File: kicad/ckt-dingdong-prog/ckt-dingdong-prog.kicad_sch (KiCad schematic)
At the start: 5 parts, among them J1 Conn_02x05_Counter_Clockwise, J2 Conn_AVR_TagConnect_TC2030, J3 Conn_01x11, J4 Conn_01x11, SW1 JS202011SCQN

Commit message: Programming board PCB complete
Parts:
- J3, J4: footprint (none) -> Connector_PinHeader_2.54mm:PinHeader_1x11_P2.54mm_Vertical
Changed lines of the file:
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@@
   (symbol (lib_id "power:GND") (at 63.5 96.52 0) (unit 1)
     (in_bom yes) (on_board yes)
-    (property "Reference" "#PWR?" (id 0) (at 63.5 102.87 0)
+    (property "Reference" "#PWR0104" (id 0) (at 63.5 102.87 0)
       (effects (font (size 1.27 1.27)) hide)
     )
@@
     (property "Reference" "J4" (id 0) (at 196.215 74.295 0))
     (property "Value" "Conn_01x11" (id 1) (at 196.215 76.835 0))
-    (property "Footprint" "" (id 2) (at 196.215 92.71 0)
+    (property "Footprint" "Connector_PinHeader_2.54mm:PinHeader_1x11_P2.54mm_Vertical" (id 2) (at 196.215 92.71 0)
       (effects (font (size 1.27 1.27)) hide)
     )
@@
   (symbol (lib_id "power:+3.3V") (at 169.545 78.74 0) (unit 1)
     (in_bom yes) (on_board yes)
-    (property "Reference" "#PWR?" (id 0) (at 169.545 82.55 0)
+    (property "Reference" "#PWR0106" (id 0) (at 169.545 82.55 0)
       (effects (font (size 1.27 1.27)) hide)
     )
@@
   (symbol (lib_id "power:GND") (at 109.855 95.25 0) (unit 1)
     (in_bom yes) (on_board yes)
-    (property "Reference" "#PWR?" (id 0) (at 109.855 101.6 0)
+    (property "Reference" "#PWR0102" (id 0) (at 109.855 101.6 0)
       (effects (font (size 1.27 1.27)) hide)
     )
@@
       (effects (font (size 1.27 1.27)) (justify left))
     )
-    (property "Footprint" "" (id 2) (at 179.07 92.71 0)
+    (property "Footprint" "Connector_PinHeader_2.54mm:PinHeader_1x11_P2.54mm_Vertical" (id 2) (at 179.07 92.71 0)
       (effects (font (size 1.27 1.27)) hide)
     )
@@
   (symbol (lib_id "power:GND") (at 78.105 120.015 0) (mirror y) (unit 1)
     (in_bom yes) (on_board yes)
-    (property "Reference" "#PWR?" (id 0) (at 78.105 126.365 0)
+    (property "Reference" "#PWR0101" (id 0) (at 78.105 126.365 0)
       (effects (font (size 1.27 1.27)) hide)
     )
@@
   (symbol (lib_id "power:+3.3V") (at 63.5 76.2 0) (unit 1)
     (in_bom yes) (on_board yes)
-    (property "Reference" "#PWR?" (id 0) (at 63.5 80.01 0)
+    (property "Reference" "#PWR0105" (id 0) (at 63.5 80.01 0)
       (effects (font (size 1.27 1.27)) hide)
     )
@@
   (symbol (lib_id "power:GND") (at 170.815 85.09 270) (unit 1)
     (in_bom yes) (on_board yes)
-    (property "Reference" "#PWR?" (id 0) (at 164.465 85.09 0)
+    (property "Reference" "#PWR0107" (id 0) (at 164.465 85.09 0)
       (effects (font (size 1.27 1.27)) hide)
     )
@@
   (symbol (lib_id "power:+3.3V") (at 109.855 82.55 0) (unit 1)
     (in_bom yes) (on_board yes)
-    (property "Reference" "#PWR?" (id 0) (at 109.855 86.36 0)
+    (property "Reference" "#PWR0103" (id 0) (at 109.855 86.36 0)
       (effects (font (size 1.27 1.27)) hide)
     )
@@
   (symbol (lib_id "power:GND") (at 204.47 80.01 90) (mirror x) (unit 1)
     (in_bom yes) (on_board yes)
-    (property "Reference" "#PWR?" (id 0) (at 210.82 80.01 0)
+    (property "Reference" "#PWR0108" (id 0) (at 210.82 80.01 0)
       (effects (font (size 1.27 1.27)) hide)
     )
@@
   )
   (symbol_instances
+    (path "/ac5e832f-5605-4361-b104-da0c11386df5"
+      (reference "#PWR0101") (unit 1) (value "GND") (footprint "")
+    )
+    (path "/89dfde83-0d62-45cd-b799-a7d2e3d1022f"
+      (reference "#PWR0102") (unit 1) (value "GND") (footprint "")
+    )
+    (path "/d3241dde-1c6a-4b3c-95fc-28b0e3d1ac80"
+      (reference "#PWR0103") (unit 1) (value "+3.3V") (footprint "")
+    )
     (path "/0b9acb28-32d4-442e-9524-2d3eb05627b8"
-      (reference "#PWR?") (unit 1) (value "GND") (footprint "")
+      (reference "#PWR0104") (unit 1) (value "GND") (footprint "")
+    )
+    (path "/c6647ba0-c558-4447-9e8b-33e9e0feb743"
+      (reference "#PWR0105") (unit 1) (value "+3.3V") (footprint "")
     )
     (path "/758fb082-f9c9-402b-b437-3ba76bb58b5f"
-      (reference "#PWR?") (unit 1) (value "+3.3V") (footprint "")
-    )
-    (path "/89dfde83-0d62-45cd-b799-a7d2e3d1022f"
-      (reference "#PWR?") (unit 1) (value "GND") (footprint "")
-    )
-    (path "/ac5e832f-5605-4361-b104-da0c11386df5"
-      (reference "#PWR?") (unit 1) (value "GND") (footprint "")
-    )
-    (path "/c6647ba0-c558-4447-9e8b-33e9e0feb743"
-      (reference "#PWR?") (unit 1) (value "+3.3V") (footprint "")
+      (reference "#PWR0106") (unit 1) (value "+3.3V") (footprint "")
     )
     (path "/c715221c-9e91-48a6-9aea-e37fd69b179b"
-      (reference "#PWR?") (unit 1) (value "GND") (footprint "")
-    )
-    (path "/d3241dde-1c6a-4b3c-95fc-28b0e3d1ac80"
-      (reference "#PWR?") (unit 1) (value "+3.3V") (footprint "")
+      (reference "#PWR0107") (unit 1) (value "GND") (footprint "")
     )
     (path "/e29628f6-5145-4926-87fe-69f2c0894165"
-      (reference "#PWR?") (unit 1) (value "GND") (footprint "")
+      (reference "#PWR0108") (unit 1) (value "GND") (footprint "")
     )
     (path "/5f39442f-fdeb-4900-b9f4-b34ab407a918"
@@
     )
     (path "/a30fa920-d39f-4c3f-8180-704f1a85a554"
-      (reference "J3") (unit 1) (value "Conn_01x11") (footprint "")
+      (reference "J3") (unit 1) (value "Conn_01x11") (footprint "Connector_PinHeader_2.54mm:PinHeader_1x11_P2.54mm_Vertical")
     )
     (path "/1cfdb6c4-1482-404e-900f-738ccb5046ef"
-      (reference "J4") (unit 1) (value "Conn_01x11") (footprint "")
+      (reference "J4") (unit 1) (value "Conn_01x11") (footprint "Connector_PinHeader_2.54mm:PinHeader_1x11_P2.54mm_Vertical")
     )
     (path "/4bc4b1ea-398b-4e60-a693-362841a5cba9"

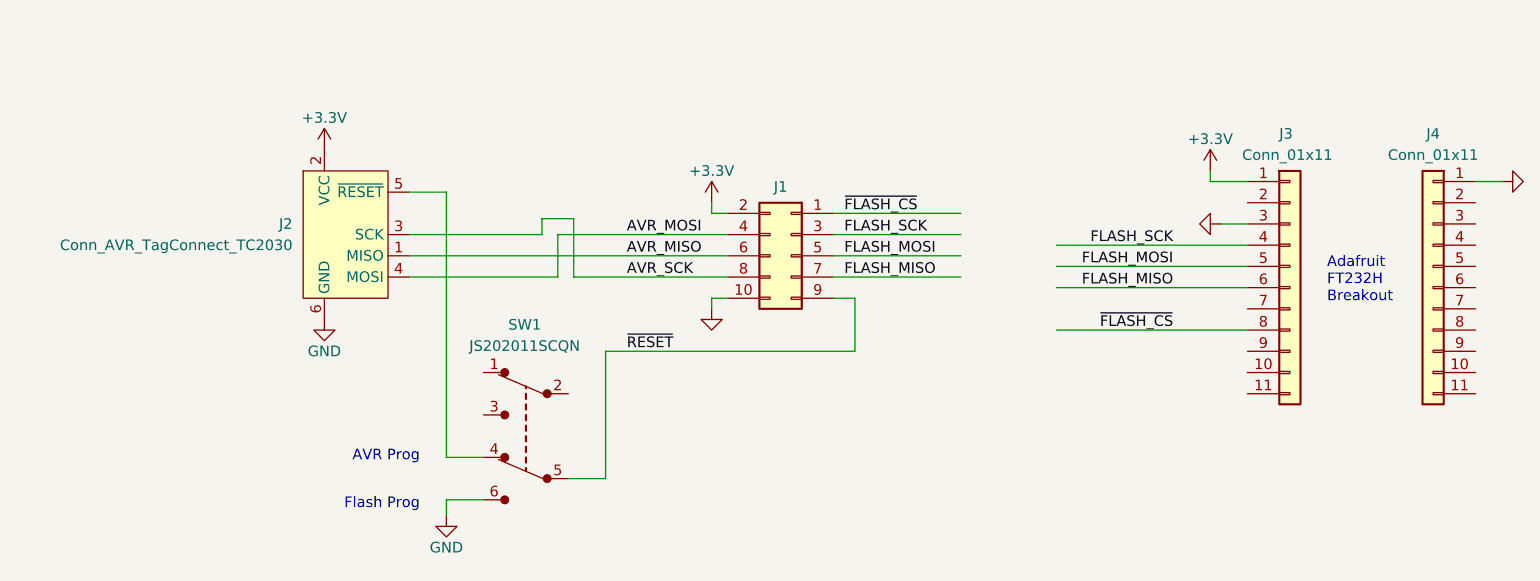
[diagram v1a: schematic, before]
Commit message: Fixed programming header
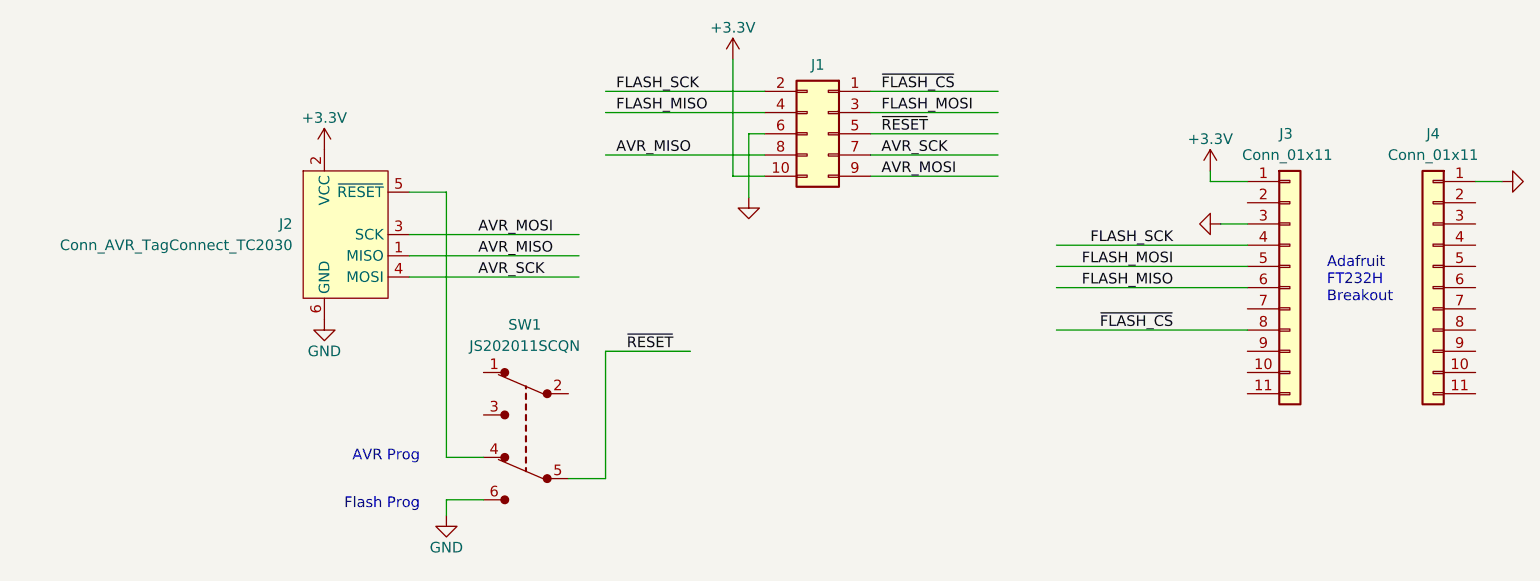
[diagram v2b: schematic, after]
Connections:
- net +3.3V: now also J1.10 (Pin_10); no longer J1.2 (Pin_2)
- net AVR_MISO: now also J1.8 (Pin_8); no longer J1.6 (Pin_6)
- net AVR_MOSI: now also J1.9 (Pin_9), J2.3 (SCK); no longer J1.4 (Pin_4), J2.4 (MOSI)
- net AVR_SCK: now also J1.7 (Pin_7), J2.4 (MOSI); no longer J1.8 (Pin_8), J2.3 (SCK)
- net FLASH_MISO: now also J1.4 (Pin_4); no longer J1.7 (Pin_7)
- net FLASH_MOSI: now also J1.3 (Pin_3); no longer J1.5 (Pin_5)
- net FLASH_SCK: now also J1.2 (Pin_2); no longer J1.3 (Pin_3)
- net GND: now also J1.6 (Pin_6); no longer J1.10 (Pin_10)
- net ~{RESET}: now also J1.5 (Pin_5); no longer J1.9 (Pin_9)

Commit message: Update programmer to fix SCK / MISO reversal, now v1.2
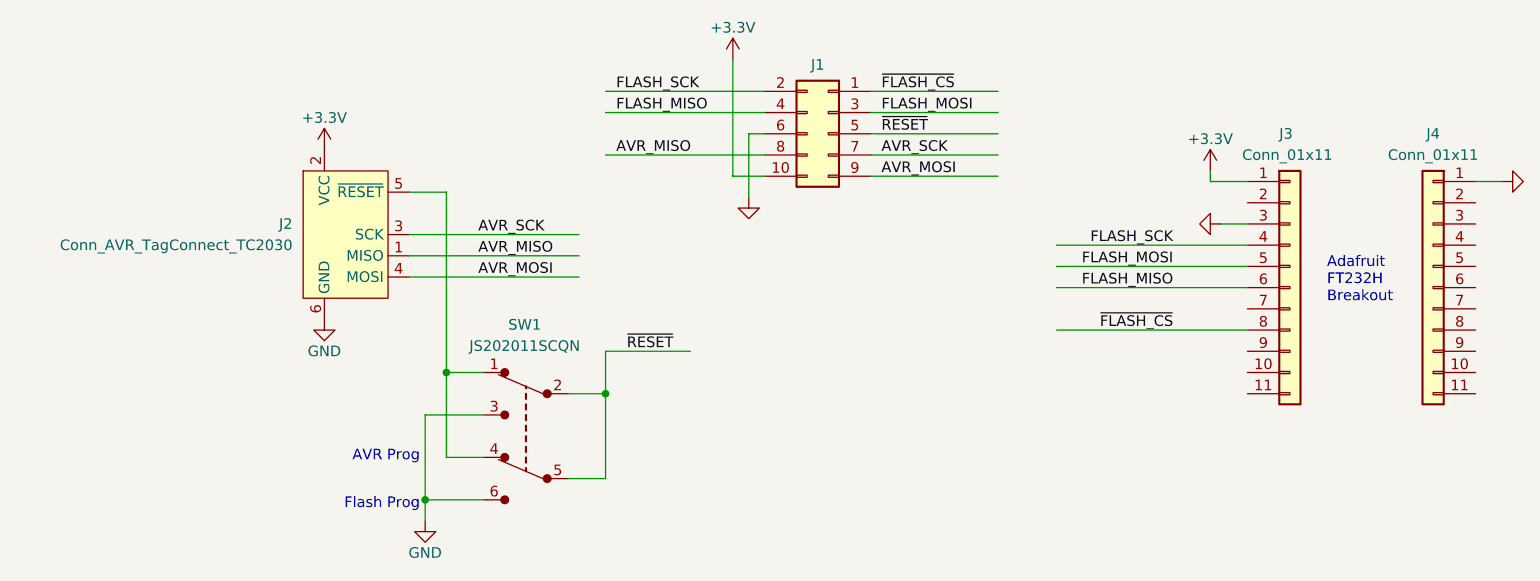
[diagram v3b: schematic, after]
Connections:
- net AVR_MOSI: now also J2.4 (MOSI); no longer J2.3 (SCK)
- net AVR_SCK: now also J2.3 (SCK); no longer J2.4 (MOSI)
- net GND: now also SW1.3
- net ~{RESET}: now also SW1.2
- net at SW1.1: now also J2.5 (~{RESET}), SW1.4
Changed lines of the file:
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@@
 (kicad_sch (version 20211123) (generator eeschema)
   (paper "A4")
+  (junction (at 75.565 118.11) (diameter 0) (color 0 0 0 0)
+  )
+  (junction (at 78.105 102.87) (diameter 0) (color 0 0 0 0)
+  )
+  (junction (at 97.155 105.41) (diameter 0) (color 0 0 0 0)
+  )
   (wire (pts (xy 112.395 65.405) (xy 112.395 79.375))
     (stroke (width 0) (type default) (color 0 0 0 0))
@@
     (stroke (width 0) (type default) (color 0 0 0 0))
   )
+  (wire (pts (xy 97.155 105.41) (xy 97.155 115.57))
+    (stroke (width 0) (type default) (color 0 0 0 0))
+  )
   (wire (pts (xy 169.545 78.74) (xy 169.545 80.01))
     (stroke (width 0) (type default) (color 0 0 0 0))
   )
+  (wire (pts (xy 78.105 102.87) (xy 78.105 113.03))
+    (stroke (width 0) (type default) (color 0 0 0 0))
+  )
+  (wire (pts (xy 78.105 102.87) (xy 82.55 102.87))
+    (stroke (width 0) (type default) (color 0 0 0 0))
+  )
   (wire (pts (xy 114.3 74.295) (xy 116.205 74.295))
     (stroke (width 0) (type default) (color 0 0 0 0))
@@
     (stroke (width 0) (type default) (color 0 0 0 0))
   )
+  (wire (pts (xy 92.71 105.41) (xy 97.155 105.41))
+    (stroke (width 0) (type default) (color 0 0 0 0))
+  )
+  (wire (pts (xy 75.565 107.95) (xy 82.55 107.95))
+    (stroke (width 0) (type default) (color 0 0 0 0))
+  )
   (wire (pts (xy 112.395 79.375) (xy 116.205 79.375))
     (stroke (width 0) (type default) (color 0 0 0 0))
@@
     (stroke (width 0) (type default) (color 0 0 0 0))
   )
-  (wire (pts (xy 78.105 81.28) (xy 78.105 113.03))
+  (wire (pts (xy 75.565 118.11) (xy 75.565 107.95))
+    (stroke (width 0) (type default) (color 0 0 0 0))
+  )
+  (wire (pts (xy 78.105 81.28) (xy 78.105 102.87))
     (stroke (width 0) (type default) (color 0 0 0 0))
   )
@@
     (stroke (width 0) (type default) (color 0 0 0 0))
   )
-  (wire (pts (xy 78.105 118.11) (xy 78.105 120.015))
-    (stroke (width 0) (type default) (color 0 0 0 0))
-  )
   (wire (pts (xy 128.905 69.215) (xy 144.145 69.215))
     (stroke (width 0) (type default) (color 0 0 0 0))
   )
-  (wire (pts (xy 78.105 118.11) (xy 82.55 118.11))
+  (wire (pts (xy 75.565 120.65) (xy 75.565 118.11))
+    (stroke (width 0) (type default) (color 0 0 0 0))
+  )
+  (wire (pts (xy 75.565 118.11) (xy 82.55 118.11))
     (stroke (width 0) (type default) (color 0 0 0 0))
   )
@@
     (stroke (width 0) (type default) (color 0 0 0 0))
   )
-  (wire (pts (xy 97.155 100.33) (xy 97.155 115.57))
+  (wire (pts (xy 97.155 100.33) (xy 97.155 105.41))
     (stroke (width 0) (type default) (color 0 0 0 0))
   )
@@
     (effects (font (size 1.27 1.27)) (justify left bottom))
   )
-  (label "AVR_MOSI" (at 81.915 86.36 0)
+  (label "AVR_SCK" (at 81.915 86.36 0)
     (effects (font (size 1.27 1.27)) (justify left bottom))
   )
@@
     (effects (font (size 1.27 1.27)) (justify left bottom))
   )
-  (label "AVR_SCK" (at 81.915 91.44 0)
+  (label "AVR_MOSI" (at 81.915 91.44 0)
     (effects (font (size 1.27 1.27)) (justify left bottom))
   )
@@
     (pin "9")
   )
-  (symbol (lib_id "power:GND") (at 78.105 120.015 0) (mirror y) (unit 1)
-    (in_bom yes) (on_board yes)
-    (property "Reference" "#PWR0101" (id 0) (at 78.105 126.365 0)
-      (effects (font (size 1.27 1.27)) hide)
-    )
-    (property "Value" "GND" (id 1) (at 78.105 123.825 0))
-    (property "Footprint" "" (id 2) (at 78.105 120.015 0)
-      (effects (font (size 1.27 1.27)) hide)
-    )
-    (property "Datasheet" "" (id 3) (at 78.105 120.015 0)
+  (symbol (lib_id "power:GND") (at 75.565 120.65 0) (mirror y) (unit 1)
+    (in_bom yes) (on_board yes)
+    (property "Reference" "#PWR0101" (id 0) (at 75.565 127 0)
+      (effects (font (size 1.27 1.27)) hide)
+    )
+    (property "Value" "GND" (id 1) (at 75.565 124.46 0))
+    (property "Footprint" "" (id 2) (at 75.565 120.65 0)
+      (effects (font (size 1.27 1.27)) hide)
+    )
+    (property "Datasheet" "" (id 3) (at 75.565 120.65 0)
       (effects (font (size 1.27 1.27)) hide)
     )
@@
   (symbol (lib_id "power:GND") (at 114.3 81.915 0) (unit 1)
     (in_bom yes) (on_board yes)
-    (property "Reference" "#PWR?" (id 0) (at 114.3 88.265 0)
+    (property "Reference" "#PWR0102" (id 0) (at 114.3 88.265 0)
       (effects (font (size 1.27 1.27)) hide)
     )
@@
   (symbol (lib_id "power:+3.3V") (at 112.395 65.405 0) (unit 1)
     (in_bom yes) (on_board yes)
-    (property "Reference" "#PWR?" (id 0) (at 112.395 69.215 0)
+    (property "Reference" "#PWR0103" (id 0) (at 112.395 69.215 0)
       (effects (font (size 1.27 1.27)) hide)
     )
@@
       (reference "#PWR0101") (unit 1) (value "GND") (footprint "")
     )
+    (path "/d1edde0a-bab3-4663-a288-39fb007e4504"
+      (reference "#PWR0102") (unit 1) (value "GND") (footprint "")
+    )
+    (path "/ea9e8e59-a99f-4b19-9d69-32885411489c"
+      (reference "#PWR0103") (unit 1) (value "+3.3V") (footprint "")
+    )
     (path "/0b9acb28-32d4-442e-9524-2d3eb05627b8"
       (reference "#PWR0104") (unit 1) (value "GND") (footprint "")
@@
       (reference "#PWR0108") (unit 1) (value "GND") (footprint "")
     )
-    (path "/d1edde0a-bab3-4663-a288-39fb007e4504"
-      (reference "#PWR?") (unit 1) (value "GND") (footprint "")
-    )
-    (path "/ea9e8e59-a99f-4b19-9d69-32885411489c"
-      (reference "#PWR?") (unit 1) (value "+3.3V") (footprint "")
-    )
     (path "/72c06044-255c-447c-a975-8c718c6f3e58"
